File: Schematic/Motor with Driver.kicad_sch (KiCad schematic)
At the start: 9 parts, among them U16 DRV8243SQDGQRQ1 (S-Variant)

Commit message: 1st Schematic Review
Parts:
- removed R139: 10k, symbol Device:R
- renumbered C171 to C172, C172 to C173, C173 to C174, C174 to C175, U16 to U19
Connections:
- net MOTORx_SCLK renamed SPI_SCLK
- net MOTORx_SDI renamed SPI_SDI
- net MOTORx_SDO renamed SPI_SDO
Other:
- note added: "Motor Current = I_IPROPI x A_IPROPI Motor Current = 0.0039 A x 3075 Motor Current ≈ 12 A"
- note added: "need a pullup on this line"

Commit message: updates
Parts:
- renumbered C172 to C174, C173 to C175, C174 to C176, C175 to C177, D43 to D45, R140 to R153, R141 to R154

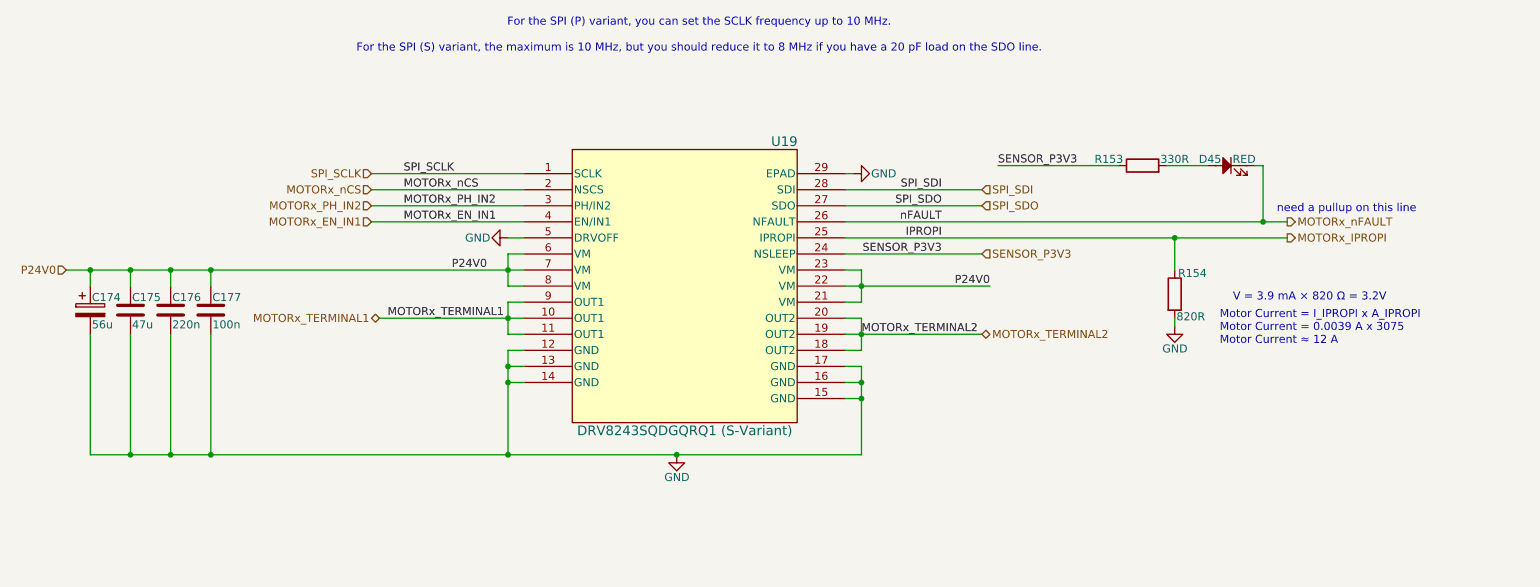
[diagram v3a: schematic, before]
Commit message: updated fuel guage
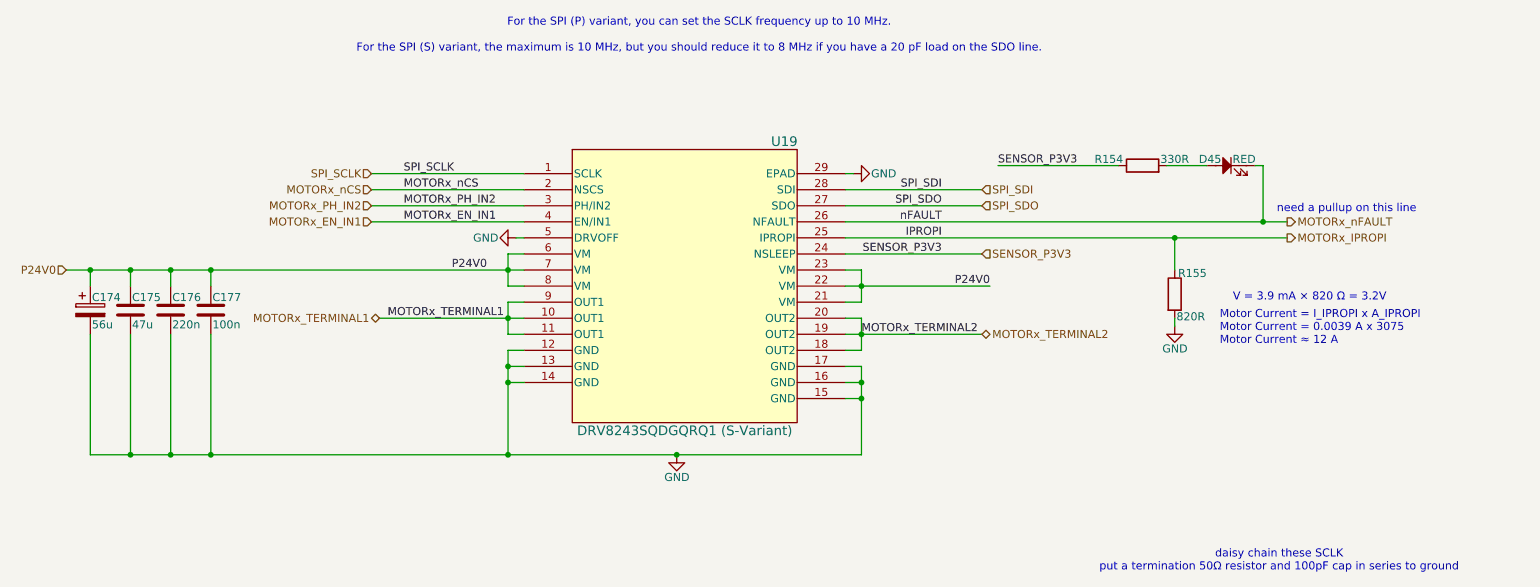
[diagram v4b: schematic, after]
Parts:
- renumbered R153 to R154, R154 to R155
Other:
- note added: "daisy chain these SCLK put a termination 50Ω resistor and 100pF cap in series to ground"
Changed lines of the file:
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@@
 		)
 	)
+	(text "daisy chain these SCLK\nput a termination 50Ω resistor and 100pF cap in series to ground"
+		(exclude_from_sim no)
+		(at 238.76 137.414 0)
+		(effects
+			(font
+				(size 1.27 1.27)
+			)
+		)
+	)
 	(text "Motor Current = I_IPROPI x A_IPROPI\nMotor Current = 0.0039 A x 3075\nMotor Current ≈ 12 A\n\n"
 		(exclude_from_sim no)
@@
 	(wire
 		(pts
-			(xy 116.84 86.36) (xy 119.38 86.36)
+			(xy 118.11 86.36) (xy 119.38 86.36)
 		)
 		(stroke
@@
 		(on_board yes)
 		(dnp no)
-		(property "Reference" "R154"
+		(property "Reference" "R155"
 			(at 225.044 91.948 0)
 			(effects
@@
 			(project "STAR"
 				(path "/fc8533bc-25dd-4c20-9b4c-ffebebd6739b/f73d6367-f3ba-42df-a3ea-bd155f1c219f/07712c52-f5ae-4a00-8c08-8de30640eab9/12332cca-8dae-4b9a-a306-a89e304a2f02"
-					(reference "R158")
+					(reference "R159")
 					(unit 1)
 				)
 				(path "/fc8533bc-25dd-4c20-9b4c-ffebebd6739b/f73d6367-f3ba-42df-a3ea-bd155f1c219f/07712c52-f5ae-4a00-8c08-8de30640eab9/7a91eb0b-b549-46c5-8b0e-dbd0b5aceef7"
-					(reference "R156")
+					(reference "R157")
 					(unit 1)
 				)
 				(path "/fc8533bc-25dd-4c20-9b4c-ffebebd6739b/f73d6367-f3ba-42df-a3ea-bd155f1c219f/07712c52-f5ae-4a00-8c08-8de30640eab9/843d6ab8-aee5-4b9b-9eb5-61d6831c2a8c"
-					(reference "R154")
+					(reference "R155")
 					(unit 1)
 				)
 				(path "/fc8533bc-25dd-4c20-9b4c-ffebebd6739b/f73d6367-f3ba-42df-a3ea-bd155f1c219f/07712c52-f5ae-4a00-8c08-8de30640eab9/ffd511cd-348c-4aa2-92a6-874df4b88d02"
-					(reference "R160")
+					(reference "R161")
 					(unit 1)
 				)
@@
 	(symbol
 		(lib_id "power:GND")
-		(at 116.84 86.36 270)
+		(at 118.11 86.36 270)
 		(unit 1)
 		(exclude_from_sim no)
@@
 		(dnp no)
 		(property "Reference" "#PWR087"
-			(at 110.49 86.36 0)
+			(at 111.76 86.36 0)
 			(effects
 				(font
@@
 		)
 		(property "Value" "GND"
-			(at 114.046 86.36 90)
+			(at 115.316 86.36 90)
 			(effects
 				(font
@@
 		)
 		(property "Footprint" ""
-			(at 116.84 86.36 0)
+			(at 118.11 86.36 0)
 			(effects
 				(font
@@
 		)
 		(property "Datasheet" ""
-			(at 116.84 86.36 0)
+			(at 118.11 86.36 0)
 			(effects
 				(font
@@
 		)
 		(property "Description" "Power symbol creates a global label with name \"GND\" , ground"
-			(at 116.84 86.36 0)
+			(at 118.11 86.36 0)
 			(effects
 				(font
@@
 		(on_board yes)
 		(dnp no)
-		(property "Reference" "R153"
+		(property "Reference" "R154"
 			(at 211.836 73.914 90)
 			(effects
@@
 			(project "STAR"
 				(path "/fc8533bc-25dd-4c20-9b4c-ffebebd6739b/f73d6367-f3ba-42df-a3ea-bd155f1c219f/07712c52-f5ae-4a00-8c08-8de30640eab9/12332cca-8dae-4b9a-a306-a89e304a2f02"
-					(reference "R157")
+					(reference "R158")
 					(unit 1)
 				)
 				(path "/fc8533bc-25dd-4c20-9b4c-ffebebd6739b/f73d6367-f3ba-42df-a3ea-bd155f1c219f/07712c52-f5ae-4a00-8c08-8de30640eab9/7a91eb0b-b549-46c5-8b0e-dbd0b5aceef7"
-					(reference "R155")
+					(reference "R156")
 					(unit 1)
 				)
 				(path "/fc8533bc-25dd-4c20-9b4c-ffebebd6739b/f73d6367-f3ba-42df-a3ea-bd155f1c219f/07712c52-f5ae-4a00-8c08-8de30640eab9/843d6ab8-aee5-4b9b-9eb5-61d6831c2a8c"
-					(reference "R153")
+					(reference "R154")
 					(unit 1)
 				)
 				(path "/fc8533bc-25dd-4c20-9b4c-ffebebd6739b/f73d6367-f3ba-42df-a3ea-bd155f1c219f/07712c52-f5ae-4a00-8c08-8de30640eab9/ffd511cd-348c-4aa2-92a6-874df4b88d02"
-					(reference "R159")
+					(reference "R160")
 					(unit 1)
 				)

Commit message: Added MCU
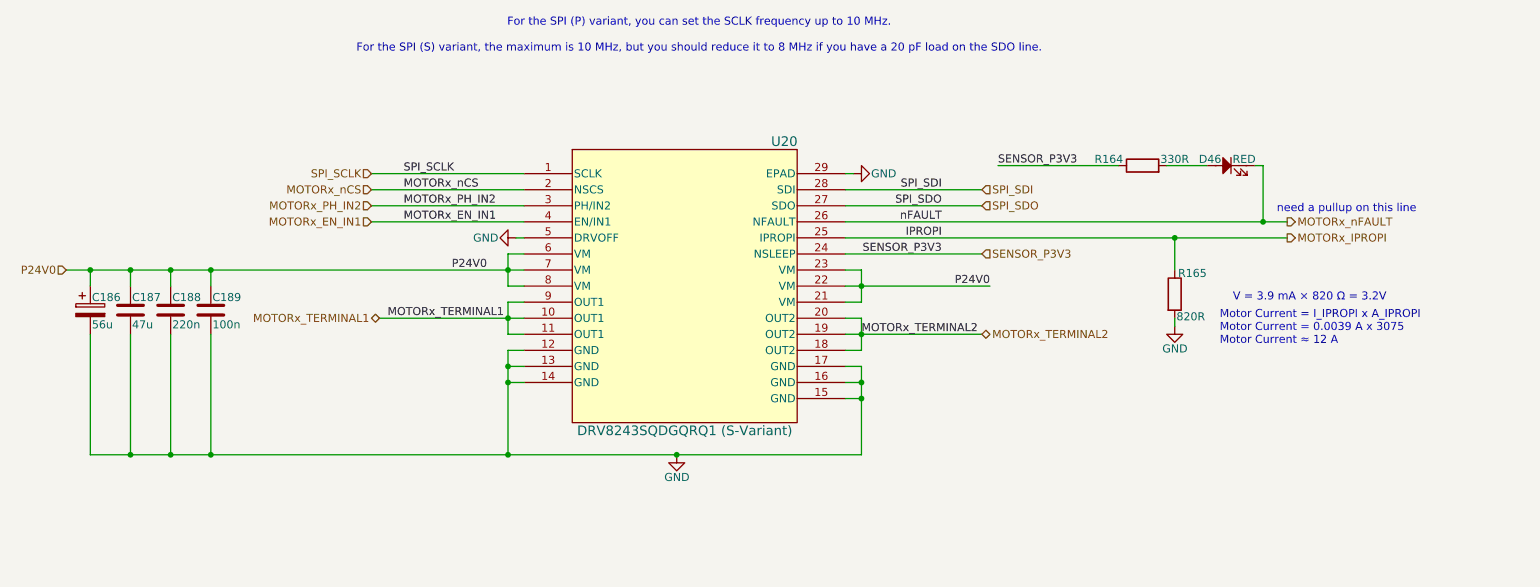
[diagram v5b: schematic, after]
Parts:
- renumbered C174 to C186, C175 to C187, C176 to C188, C177 to C189, D45 to D46, R154 to R164, R155 to R165, U19 to U20
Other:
- note removed: "daisy chain these SCLK put a termination 50Ω resistor and 100pF cap in series to ground"

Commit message: Started to work on the BOM
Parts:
- removed C186: 56u, symbol Device:C_Polarized
- removed C187: 47u, symbol Device:C
- added C185: 56u, AHA0810560M040R:CAPAE830X1100M, symbol Device:C_Polarized
- C186: renamed from C188; footprint (none) -> Capacitor_SMD:C_0805_2012Metric_Pad1.18x1.45mm_HandSolder; Link (none) -> https://mou.sr/42gipOV; Manufacturer Part Number (none) -> CL21B224KBFNFNE; Price per Unit (none) -> 0.10; Supplier (none) -> Mouser; Supplier Part Number (none) -> 187-CL21B224KBFNFNE
- C187: renamed from C189; footprint (none) -> Capacitor_SMD:C_1206_3216Metric_Pad1.33x1.80mm_HandSolder; Link (none) -> https://mou.sr/4n9ybmQ; Manufacturer Part Number (none) -> CL31B104KBCNNNC; Price per Unit (none) -> 0.11; Supplier (none) -> Mouser; Supplier Part Number (none) -> 187-CL31B104KBCNNNC
- D43: renamed from D46; footprint PCM_Diode_SMD_AKL:D_0805_2012Metric -> ASMM-CR03-BU802:LEDM3528X210N; Link (none) -> https://mou.sr/460BFB7; Manufacturer Part Number (none) -> ASMM-CR03-BU802; Price per Unit (none) -> 0.32; Supplier (none) -> Mouser; Supplier Part Number (none) -> 630-ASMM-CR03-BU802
- U18: renamed from U20; footprint VSSOP28_DGQ_TEX -> (none)
- renumbered R164 to R160, R165 to R161
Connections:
- net GND: now also C185.2
- net P24V0: now also C185.1

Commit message: Massive pivit, simplification
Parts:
- renumbered C185 to C174, C186 to C175, C187 to C176, D43 to D42, U18 to U16
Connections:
- net SENSOR_P3V3 renamed MCU_P3V3

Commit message: updated schematic
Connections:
- net SPI_SDI renamed SPI_CIPO
- net SPI_SDO renamed SPI_COPI
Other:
- note added: "For the SPI (P) variant, you can set the SCLK frequency up to 10 MHz. For the SPI (S) variant, the maximum is 10 MHz, but you should reduce it to 8 MHz if you have a 20 pF load on the COPI line."
- note removed: "For the SPI (P) variant, you can set the SCLK frequency up to 10 MHz. For the SPI (S) variant, the maximum is 10 MHz, but you should reduce it to 8 MHz if you have a 20 pF load on the SDO line."
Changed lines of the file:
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@@
 		)
 	)
-	(text "For the SPI (P) variant, you can set the SCLK frequency up to 10 MHz.\n\nFor the SPI (S) variant, the maximum is 10 MHz, but you should reduce it to 8 MHz if you have a 20 pF load on the SDO line."
+	(text "For the SPI (P) variant, you can set the SCLK frequency up to 10 MHz.\n\nFor the SPI (S) variant, the maximum is 10 MHz, but you should reduce it to 8 MHz if you have a 20 pF load on the COPI line."
 		(exclude_from_sim no)
 		(at 147.066 54.356 0)
@@
 		)
 	)
-	(label "SPI_SDI"
+	(label "SPI_CIPO"
 		(at 185.42 78.74 180)
 		(effects
@@
 		)
 	)
-	(label "SPI_SDO"
+	(label "SPI_COPI"
 		(at 185.42 81.28 180)
 		(effects
@@
 		)
 	)
-	(hierarchical_label "SPI_SDO"
+	(hierarchical_label "SPI_COPI"
 		(shape input)
 		(at 191.77 81.28 0)
@@
 		)
 	)
-	(hierarchical_label "SPI_SDI"
+	(hierarchical_label "SPI_CIPO"
 		(shape input)
 		(at 191.77 78.74 0)
